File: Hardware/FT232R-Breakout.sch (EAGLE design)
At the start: 20 parts, among them U1 FT232R

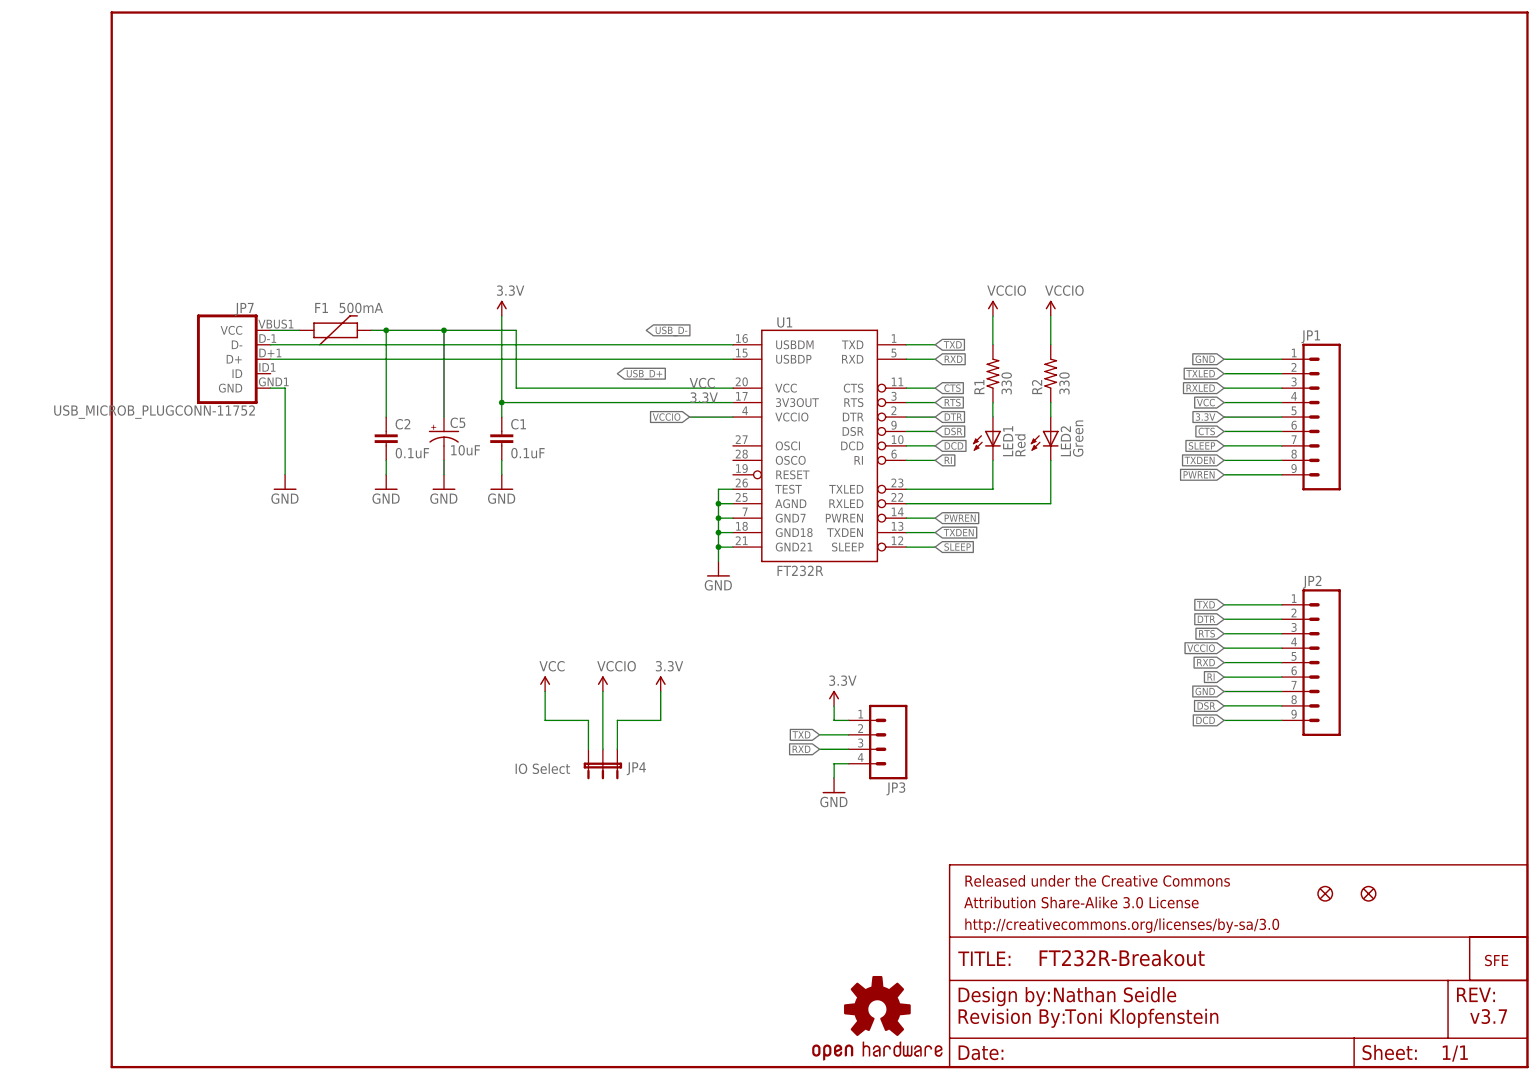
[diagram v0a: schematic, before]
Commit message: Adding SMD switch for 3.3V/ 5V selection
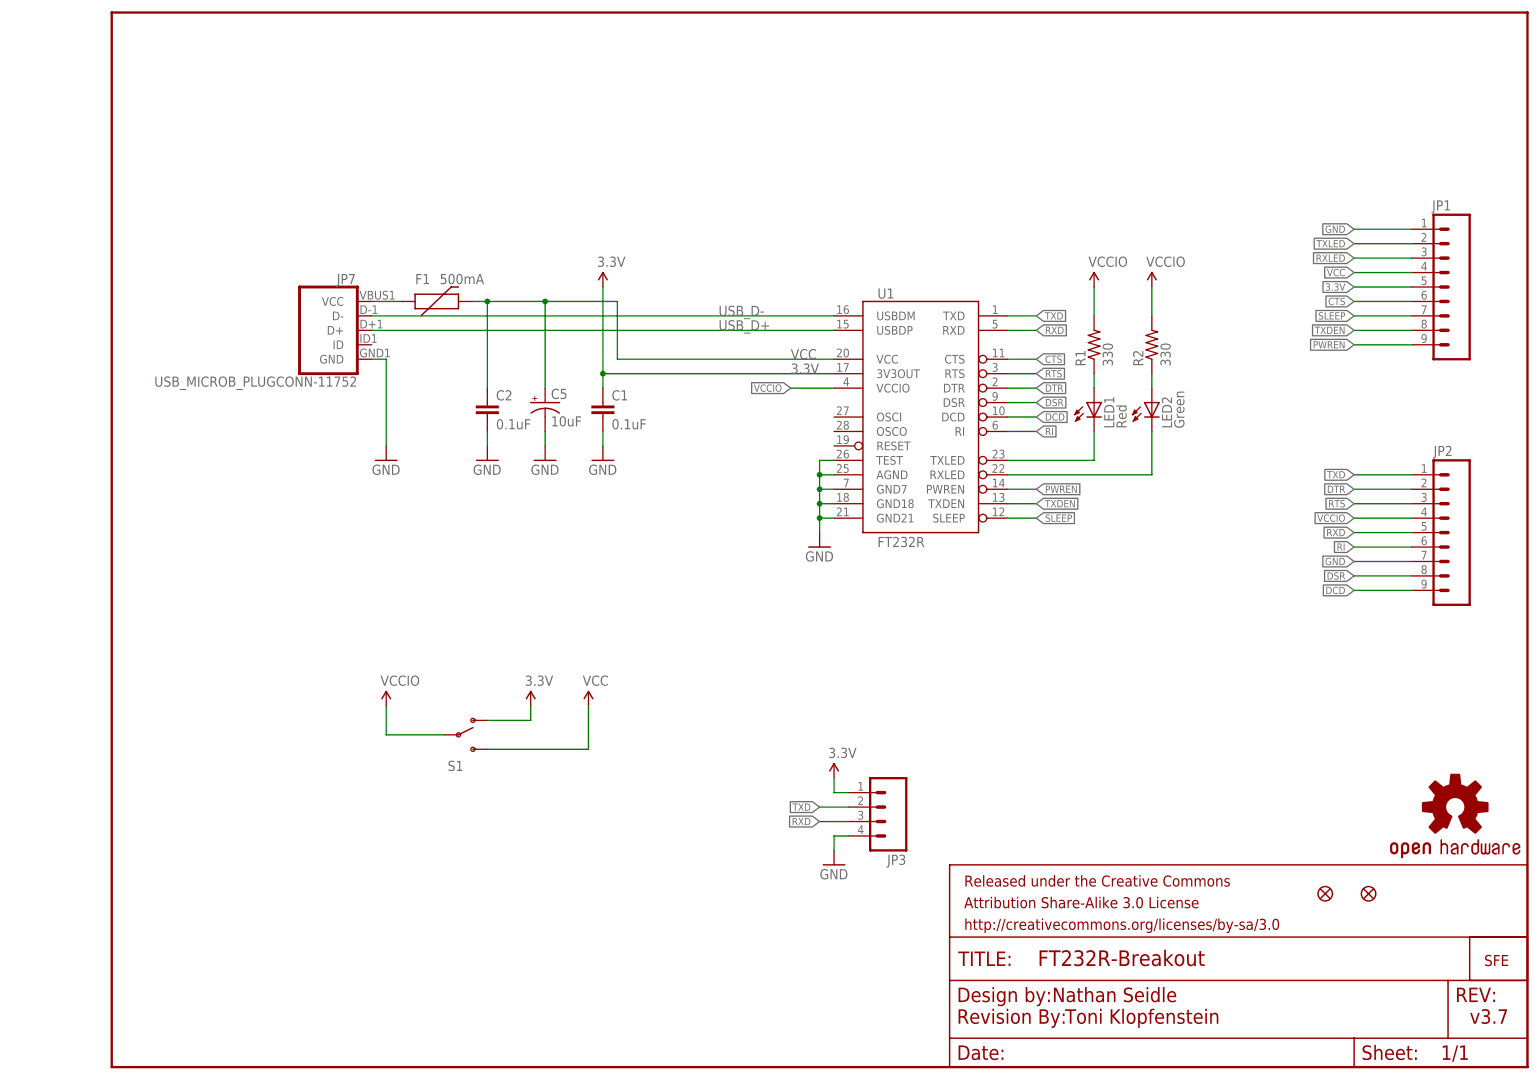
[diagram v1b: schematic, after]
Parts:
- removed JP4: IO Select, SparkFun-Passives:JUMPER-31-2
- added S1: (no value), SparkFun-Electromechanical:SWITCH-SPDTSMD
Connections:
- net 3.3V: now also S1.O; no longer JP4.1
- net VCC: now also S1.S; no longer JP4.3
- net VCCIO: now also S1.P; no longer JP4.2
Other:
- moved on the sheet: C1, C2, C5, F1, JP1, JP2, JP3, JP7, LED1, LED2, R1, R2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

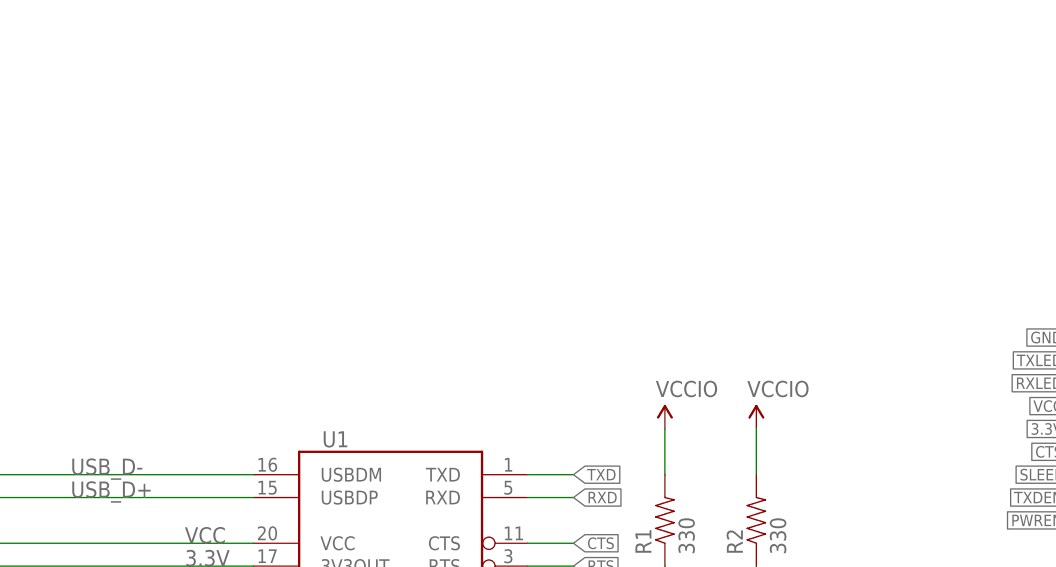
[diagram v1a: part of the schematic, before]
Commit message: Updating rev with recommendations from review
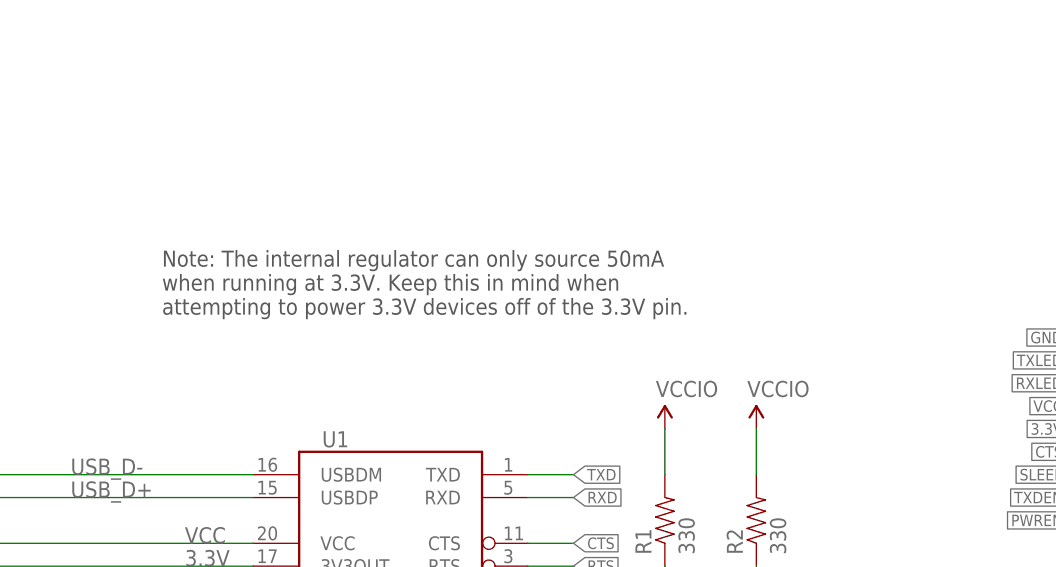
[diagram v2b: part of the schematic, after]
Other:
- note added: "Note: The internal regulator can only source 50mA when running at 3.3V. Keep this in mind when attempting to power 3.3V devices off of the 3.3V pin."
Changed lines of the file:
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@@
 <?xml version="1.0" encoding="utf-8"?>
 <!DOCTYPE eagle SYSTEM "eagle.dtd">
-<eagle version="6.4">
+<eagle version="6.5.0">
 <drawing>
 <settings>
@@
 <grid distance="0.1" unitdist="inch" unit="inch" style="lines" multiple="1" display="no" altdistance="0.01" altunitdist="inch" altunit="inch"/>
 <layers>
-<layer number="1" name="Top" color="4" fill="1" visible="no" active="no"/>
-<layer number="2" name="Route2" color="1" fill="3" visible="no" active="no"/>
-<layer number="3" name="Route3" color="4" fill="3" visible="no" active="no"/>
-<layer number="4" name="Route4" color="1" fill="4" visible="no" active="no"/>
-<layer number="5" name="Route5" color="4" fill="4" visible="no" active="no"/>
-<layer number="6" name="Route6" color="1" fill="8" visible="no" active="no"/>
-<layer number="7" name="Route7" color="4" fill="8" visible="no" active="no"/>
-<layer number="8" name="Route8" color="1" fill="2" visible="no" active="no"/>
-<layer number="9" name="Route9" color="4" fill="2" visible="no" active="no"/>
-<layer number="10" name="Route10" color="1" fill="7" visible="no" active="no"/>
-<layer number="11" name="Route11" color="4" fill="7" visible="no" active="no"/>
-<layer number="12" name="Route12" color="1" fill="5" visible="no" active="no"/>
-<layer number="13" name="Route13" color="4" fill="5" visible="no" active="no"/>
-<layer number="14" name="Route14" color="1" fill="6" visible="no" active="no"/>
-<layer number="15" name="Route15" color="4" fill="6" visible="no" active="no"/>
-<layer number="16" name="Bottom" color="1" fill="1" visible="no" active="no"/>
-<layer number="17" name="Pads" color="2" fill="1" visible="no" active="no"/>
-<layer number="18" name="Vias" color="2" fill="1" visible="no" active="no"/>
-<layer number="19" name="Unrouted" color="6" fill="1" visible="no" active="no"/>
-<layer number="20" name="Dimension" color="15" fill="1" visible="no" active="no"/>
-<layer number="21" name="tPlace" color="15" fill="1" visible="no" active="no"/>
-<layer number="22" name="bPlace" color="14" fill="1" visible="no" active="no"/>
-<layer number="23" name="tOrigins" color="15" fill="1" visible="no" active="no"/>
-<layer number="24" name="bOrigins" color="15" fill="1" visible="no" active="no"/>
-<layer number="25" name="tNames" color="7" fill="1" visible="no" active="no"/>
-<layer number="26" name="bNames" color="7" fill="1" visible="no" active="no"/>
-<layer number="27" name="tValues" color="7" fill="1" visible="no" active="no"/>
-<layer number="28" name="bValues" color="7" fill="1" visible="no" active="no"/>
+<layer number="1" name="Top" color="4" fill="1" visible="yes" active="no"/>
+<layer number="2" name="Route2" color="1" fill="3" visible="yes" active="no"/>
+<layer number="3" name="Route3" color="4" fill="3" visible="yes" active="no"/>
+<layer number="4" name="Route4" color="1" fill="4" visible="yes" active="no"/>
+<layer number="5" name="Route5" color="4" fill="4" visible="yes" active="no"/>
+<layer number="6" name="Route6" color="1" fill="8" visible="yes" active="no"/>
+<layer number="7" name="Route7" color="4" fill="8" visible="yes" active="no"/>
+<layer number="8" name="Route8" color="1" fill="2" visible="yes" active="no"/>
+<layer number="9" name="Route9" color="4" fill="2" visible="yes" active="no"/>
+<layer number="10" name="Route10" color="1" fill="7" visible="yes" active="no"/>
+<layer number="11" name="Route11" color="4" fill="7" visible="yes" active="no"/>
+<layer number="12" name="Route12" color="1" fill="5" visible="yes" active="no"/>
+<layer number="13" name="Route13" color="4" fill="5" visible="yes" active="no"/>
+<layer number="14" name="Route14" color="1" fill="6" visible="yes" active="no"/>
+<layer number="15" name="Route15" color="4" fill="6" visible="yes" active="no"/>
+<layer number="16" name="Bottom" color="1" fill="1" visible="yes" active="no"/>
+<layer number="17" name="Pads" color="2" fill="1" visible="yes" active="no"/>
+<layer number="18" name="Vias" color="2" fill="1" visible="yes" active="no"/>
+<layer number="19" name="Unrouted" color="6" fill="1" visible="yes" active="no"/>
+<layer number="20" name="Dimension" color="6" fill="1" visible="yes" active="no"/>
+<layer number="21" name="tPlace" color="16" fill="1" visible="yes" active="no"/>
+<layer number="22" name="bPlace" color="14" fill="1" visible="yes" active="no"/>
+<layer number="23" name="tOrigins" color="15" fill="1" visible="yes" active="no"/>
+<layer number="24" name="bOrigins" color="15" fill="1" visible="yes" active="no"/>
+<layer number="25" name="tNames" color="7" fill="1" visible="yes" active="no"/>
+<layer number="26" name="bNames" color="7" fill="1" visible="yes" active="no"/>
+<layer number="27" name="tValues" color="7" fill="1" visible="yes" active="no"/>
+<layer number="28" name="bValues" color="7" fill="1" visible="yes" active="no"/>
 <layer number="29" name="tStop" color="7" fill="3" visible="no" active="no"/>
 <layer number="30" name="bStop" color="7" fill="6" visible="no" active="no"/>
@@
 <layer number="35" name="tGlue" color="7" fill="4" visible="no" active="no"/>
 <layer number="36" name="bGlue" color="7" fill="5" visible="no" active="no"/>
-<layer number="37" name="tTest" color="7" fill="1" visible="no" active="no"/>
-<layer number="38" name="bTest" color="7" fill="1" visible="no" active="no"/>
+<layer number="37" name="tTest" color="7" fill="1" visible="yes" active="no"/>
+<layer number="38" name="bTest" color="7" fill="1" visible="yes" active="no"/>
 <layer number="39" name="tKeepout" color="4" fill="11" visible="no" active="no"/>
 <layer number="40" name="bKeepout" color="1" fill="11" visible="no" active="no"/>
@@
 <layer number="44" name="Drills" color="7" fill="1" visible="no" active="no"/>
 <layer number="45" name="Holes" color="7" fill="1" visible="no" active="no"/>
-<layer number="46" name="Milling" color="3" fill="1" visible="no" active="no"/>
-<layer number="47" name="Measures" color="7" fill="1" visible="no" active="no"/>
-<layer number="48" name="Document" color="7" fill="1" visible="no" active="no"/>
-<layer number="49" name="Reference" color="7" fill="1" visible="no" active="no"/>
-<layer number="50" name="dxf" color="7" fill="1" visible="no" active="no"/>
-<layer number="51" name="tDocu" color="6" fill="1" visible="no" active="no"/>
-<layer number="52" name="bDocu" color="7" fill="1" visible="no" active="no"/>
-<layer number="53" name="tGND_GNDA" color="7" fill="9" visible="no" active="no"/>
-<layer number="54" name="bGND_GNDA" color="1" fill="9" visible="no" active="no"/>
-<layer number="56" name="wert" color="7" fill="1" visible="no" active="no"/>
+<layer number="46" name="Milling" color="3" fill="1" visible="yes" active="no"/>
+<layer number="47" name="Measures" color="7" fill="1" visible="yes" active="no"/>
+<layer number="48" name="Document" color="7" fill="1" visible="yes" active="no"/>
+<layer number="49" name="Reference" color="7" fill="1" visible="yes" active="no"/>
+<layer number="50" name="dxf" color="7" fill="1" visible="yes" active="no"/>
+<layer number="51" name="tDocu" color="6" fill="1" visible="yes" active="no"/>
+<layer number="52" name="bDocu" color="7" fill="1" visible="yes" active="no"/>
+<layer number="53" name="tGND_GNDA" color="7" fill="9" visible="yes" active="no"/>
+<layer number="54" name="bGND_GNDA" color="1" fill="9" visible="yes" active="no"/>
+<layer number="56" name="wert" color="7" fill="1" visible="yes" active="no"/>
 <layer number="91" name="Nets" color="2" fill="1" visible="yes" active="yes"/>
 <layer number="92" name="Busses" color="1" fill="1" visible="yes" active="yes"/>
@@
 <text x="165.354" y="11.43" size="2.54" layer="94">Nathan Seidle</text>
 <text x="167.64" y="7.62" size="2.54" layer="94">Toni Klopfenstein</text>
+<text x="116.84" y="149.86" size="1.778" layer="97">Note: The internal regulator can only source 50mA
+when running at 3.3V. Keep this in mind when
+attempting to power 3.3V devices off of the 3.3V pin. </text>
 </plain>
 <instances>
@@
 </schematic>
 </drawing>
+<compatibility>
+<note version="6.3" minversion="6.2.2" severity="warning">
+Since Version 6.2.2 text objects can contain more than one line,
+which will not be processed correctly with this version.
+</note>
+</compatibility>
 </eagle>
